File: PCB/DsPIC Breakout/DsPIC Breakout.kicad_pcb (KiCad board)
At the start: 2 copper layers, 16 parts, among them J1 BREADBOARD_HEADER_16X1, J2 BREADBOARD_HEADER_16X1, J3 BREADBOARD_HEADER_16X1, J4 BREADBOARD_HEADER_16X1, P1 CONN_2, P2 PROG_H, U1 DSPIC33EP512MC806

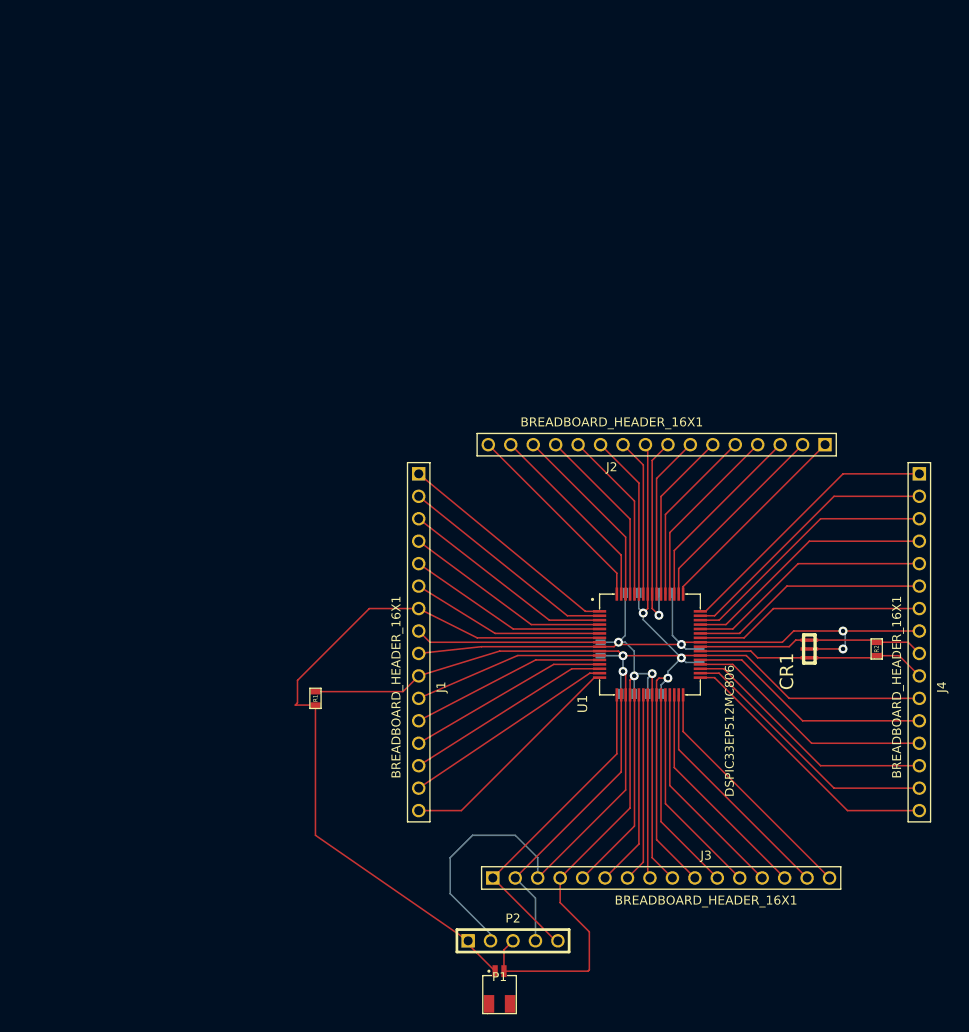
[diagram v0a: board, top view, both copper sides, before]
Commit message: Updated Breakout Board 64pin dsPIC
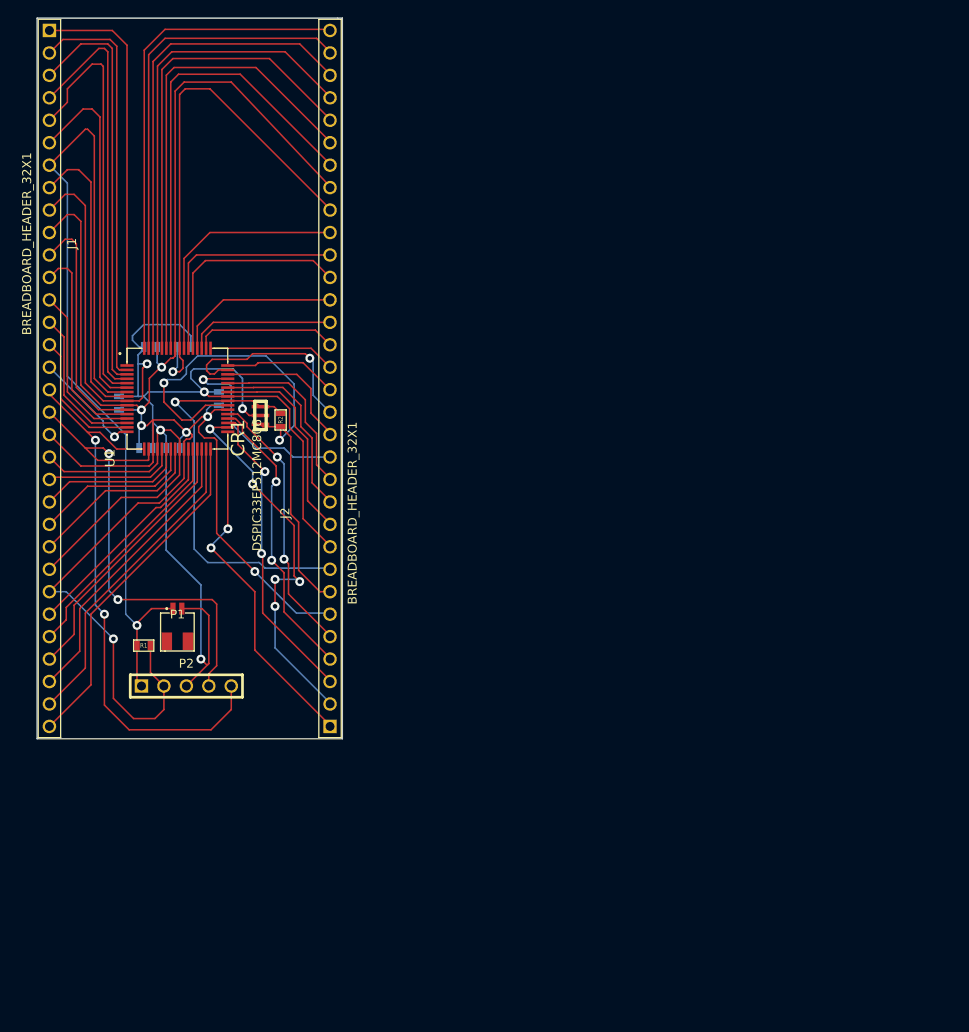
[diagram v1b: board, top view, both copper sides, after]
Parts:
- removed J3, J4: BREADBOARD_HEADER_16X1, PIN_ARRAY_16x1
- J1: value BREADBOARD_HEADER_16X1 -> BREADBOARD_HEADER_32X1; footprint PIN_ARRAY_16x1 -> PIN_ARRAY_32x1
- J2: value BREADBOARD_HEADER_16X1 -> BREADBOARD_HEADER_32X1; footprint PIN_ARRAY_16x1 -> PIN_ARRAY_32X1
- moved R2 72.2 mm to (58.3, 59.4)
- moved CR1 67.5 mm to (56.0, 58.9)
- moved J1 65.3 mm to (33.4, 39.5)
- moved C6 61.6 mm to (51.3, 57.0)
- moved C2 61.2 mm to (43.1, 62.6)
- moved C4 61.2 mm to (46.1, 62.6)
- moved C1 61.2 mm to (40.0, 57.5)
- moved C3 61.2 mm to (47.4, 51.2)
- moved C5 61.2 mm to (43.6, 51.2)
- moved U1 60.3 mm to (46.6, 57.0)
- moved P1 54.9 mm to (46.6, 82.7)
- moved P2 46.9 mm to (47.6, 89.5)
- moved J2 33.8 mm to (62.6, 70.0), turned to 90 degrees
- moved R1 20.3 mm to (42.8, 85.0), turned to 180 degrees
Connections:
- C3 pad 2: N-000003 (its old number) -> N-0000032
- CR1 pad 1: N-0000021 -> N-0000026
- CR1 pad 3: N-0000032 -> N-0000025
- J2 pad 1: N-0000031 (its old number) -> N-0000015
- J2 pad 10: N-000002 (its old number) -> N-0000018
- J2 pad 11: N-000004 (its old number) -> N-0000019
- J2 pad 12: N-0000019 -> N-0000020
- J2 pad 13: N-0000018 -> N-0000021
- J2 pad 14: N-0000017 -> N-0000022
- J2 pad 15: N-0000016 -> N-0000023
- J2 pad 16: N-0000015 -> N-0000024
- J2 pad 2: N-0000030 -> N-0000014
- J2 pad 3: N-0000028 -> N-0000013
- J2 pad 4: N-0000029 -> N-0000012
- J2 pad 5: N-0000012 -> N-0000011
- J2 pad 6: N-000005 -> VCC
- J2 pad 7: N-000001 (its old number) -> N-0000026
- J2 pad 8: N-000003 (its old number) -> N-0000025
- J2 pad 9: VCC -> GND
- P2 pad 4: N-0000055 -> N-0000052
- P2 pad 5: N-0000056 -> N-0000053
- R2 pad 1: N-0000021 -> N-0000026
- R2 pad 2: N-0000032 -> N-0000025
- U1 pad 17: N-0000056 -> N-0000053
- U1 pad 18: N-0000055 -> N-0000052
- U1 pad 21: N-0000053 -> N-0000055
- U1 pad 22: N-0000052 -> N-0000056
- U1 pad 23: N-0000051 -> N-0000054
- U1 pad 24: N-0000050 -> N-0000016
- U1 pad 27: N-0000045 -> N-000005
- U1 pad 28: N-0000046 -> N-000006
- U1 pad 29: N-0000048 -> N-0000046
- U1 pad 30: N-0000027 -> N-0000010
- U1 pad 31: N-0000026 -> N-000007
- U1 pad 32: N-000007 -> N-0000040
- U1 pad 33: N-0000025 -> N-0000015
- U1 pad 34: N-0000024 -> N-0000014
- U1 pad 35: N-0000020 -> N-0000013
- U1 pad 36: N-0000023 -> N-0000012
- U1 pad 37: N-0000022 -> N-0000011
- U1 pad 39: N-0000021 -> N-0000026
- U1 pad 40: N-0000032 -> N-0000025
- U1 pad 42: N-000008 (its old number) -> N-0000018
- U1 pad 43: N-000009 (its old number) -> N-0000019
- U1 pad 44: N-0000010 -> N-0000020
- U1 pad 45: N-0000011 -> N-0000021
- U1 pad 46: N-000006 -> N-0000022
- U1 pad 47: N-0000013 -> N-0000023
- U1 pad 48: N-0000014 -> N-0000024
- U1 pad 49: N-0000031 (its old number) -> N-0000041
- U1 pad 50: N-0000030 -> N-0000042
- U1 pad 51: N-0000028 -> N-0000043
- U1 pad 52: N-0000029 -> N-0000044
- U1 pad 53: N-0000012 -> N-0000045
- U1 pad 54: N-000005 -> N-0000047
- U1 pad 55: N-000001 (its old number) -> N-0000051
- U1 pad 56: N-000003 (its old number) -> N-0000032
- U1 pad 58: N-000002 (its old number) -> N-0000030
- U1 pad 59: N-000004 (its old number) -> N-0000028
- U1 pad 60: N-0000019 -> N-0000048
- U1 pad 61: N-0000018 -> N-0000027
- U1 pad 62: N-0000017 -> N-0000049
- U1 pad 63: N-0000016 -> N-0000029
- U1 pad 64: N-0000015 -> N-0000050
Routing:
- net N-0000049: track 0.00 -> 54.7 mm
- net N-0000053: track 23.1 -> 64.6 mm, vias 0 -> 2
- net N-0000040: track 0.00 -> 38.9 mm
- net N-0000050: track 20.8 -> 55.7 mm
- net N-0000026: track 26.7 -> 61.3 mm, vias 0 -> 2
- net N-0000029: track 21.0 -> 55.1 mm
- net GND: track 167.5 -> 201.2 mm, vias 6 -> 5
- net N-0000052: track 22.3 -> 55.6 mm, vias 0 -> 2
- net N-0000032: track 25.7 -> 58.4 mm, vias 0 -> 1
- net VCC: track 193.6 -> 225.7 mm, vias 5 -> 7
- net N-0000028: track 21.9 -> 53.2 mm
- net N-0000030: track 22.7 -> 52.7 mm
- net N-0000048: track 25.0 -> 53.9 mm
- net N-0000027: track 25.9 -> 54.2 mm
- net N-000009 (its old number): track 27.0 -> 0.00 mm
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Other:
- board outline added: 34.5 x 81.5 mm

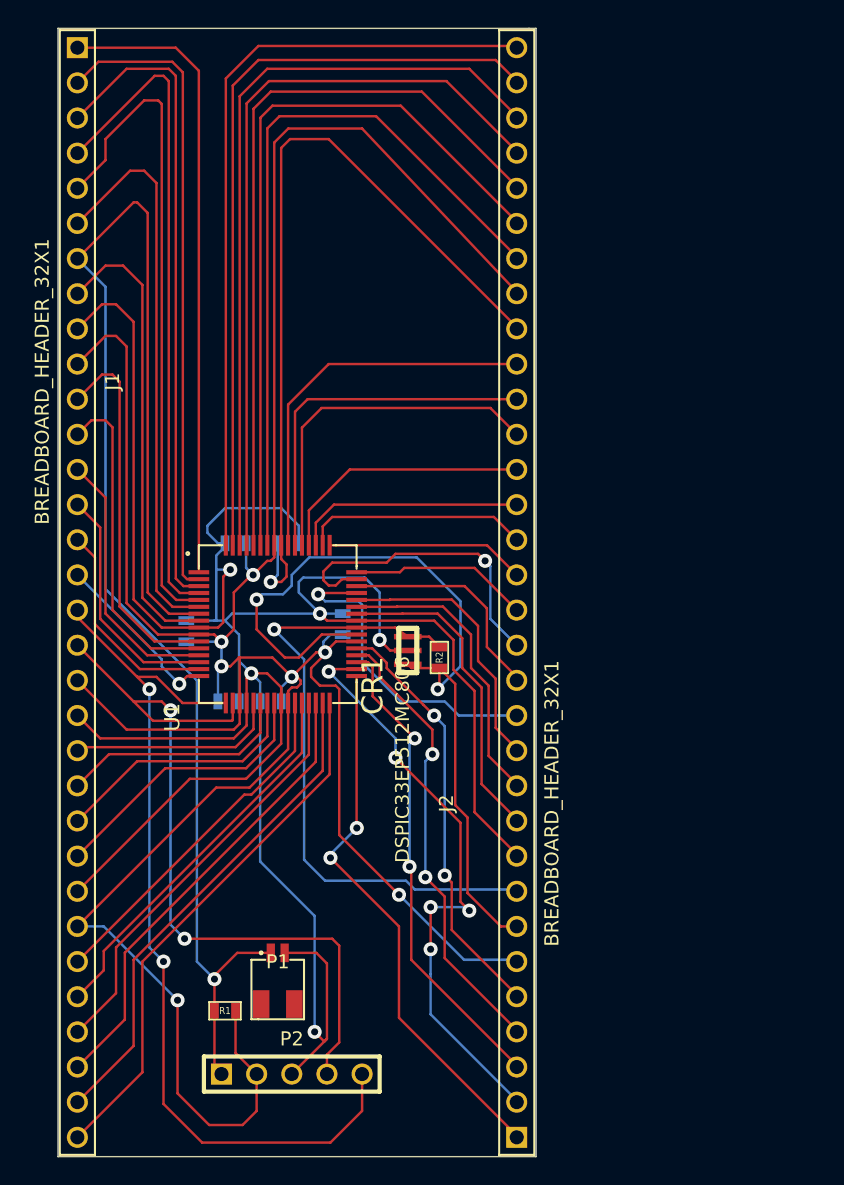
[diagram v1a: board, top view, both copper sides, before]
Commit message: BreakoutBoard 64pin dsPIC
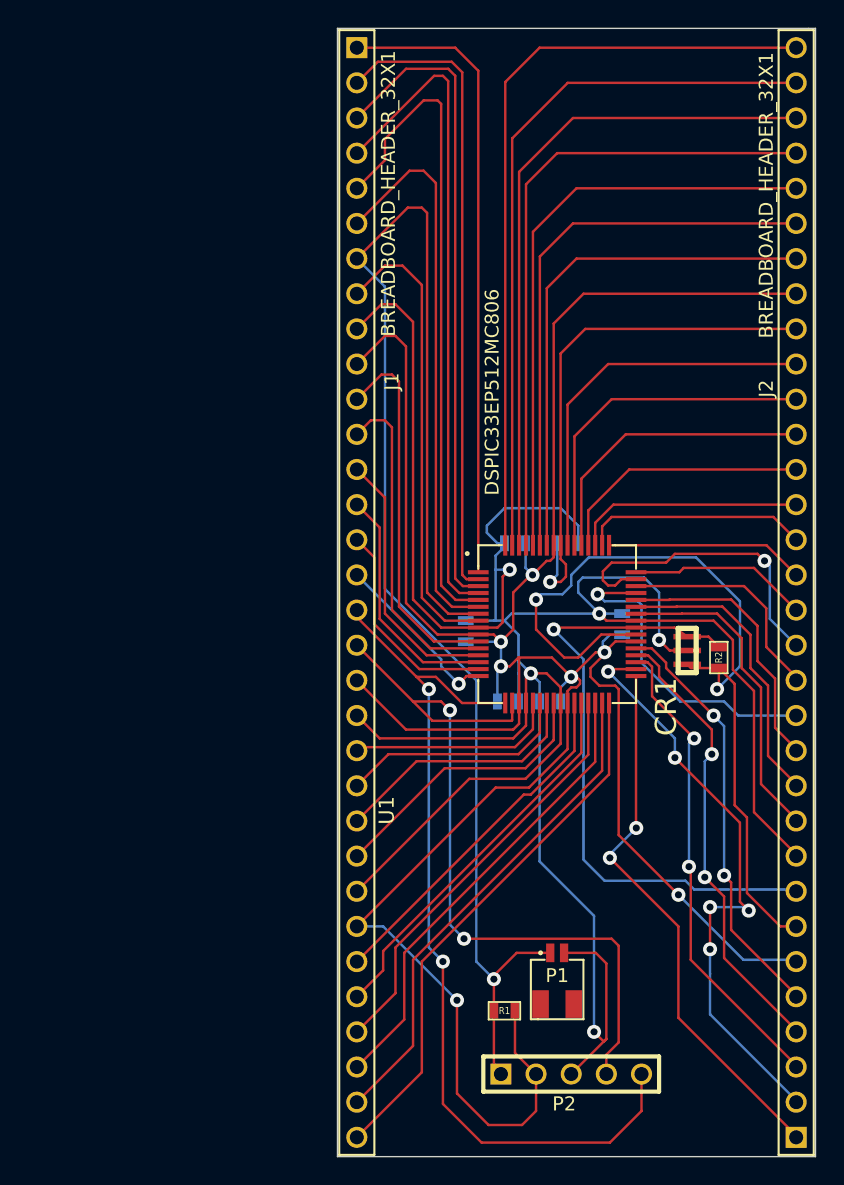
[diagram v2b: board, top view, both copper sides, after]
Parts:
- moved C2 20.2 mm to (63.2, 62.6)
- moved C6 20.2 mm to (71.5, 57.0)
- moved CR1 20.2 mm to (76.2, 58.9)
- moved J2 20.2 mm to (82.8, 70.0)
- moved P1 20.2 mm to (66.8, 82.7)
- moved R2 20.2 mm to (78.5, 59.4)
- moved U1 20.2 mm to (66.8, 57.0)
- moved C1 20.2 mm to (60.2, 57.5)
- moved C4 20.2 mm to (66.3, 62.6)
- moved C5 20.2 mm to (63.8, 51.2)
- moved J1 20.2 mm to (53.6, 39.5)
- moved P2 20.2 mm to (67.8, 89.5)
- moved R1 20.2 mm to (63.0, 85.0)
- moved C3 20.2 mm to (67.6, 51.2)
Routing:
- net N-0000032: track 58.4 -> 38.3 mm
- net VCC: track 225.7 -> 208.0 mm
- net N-0000030: track 52.7 -> 37.5 mm
- net N-0000028: track 53.2 -> 40.4 mm
- net N-0000048: track 53.9 -> 43.0 mm
- net N-0000027: track 54.2 -> 46.5 mm
- net N-0000049: track 54.7 -> 48.6 mm
- net N-0000045: track 25.4 -> 21.7 mm
- net N-0000029: track 55.1 -> 51.6 mm
- net N-0000047: track 26.0 -> 25.0 mm
